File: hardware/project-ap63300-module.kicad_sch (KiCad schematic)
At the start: 12 parts, among them U2 AP63300WU-7

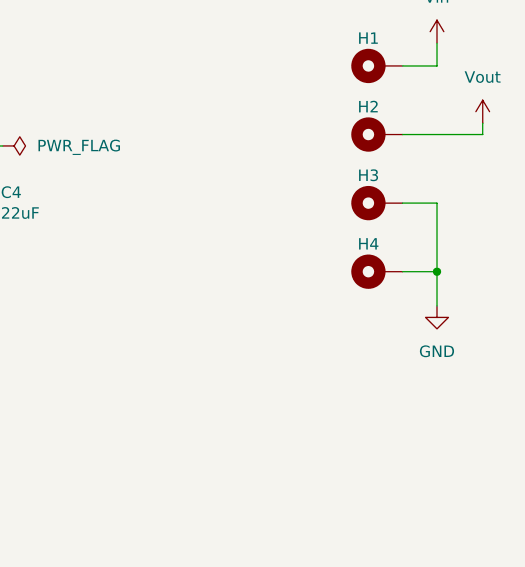
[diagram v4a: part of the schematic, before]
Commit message: Add labels
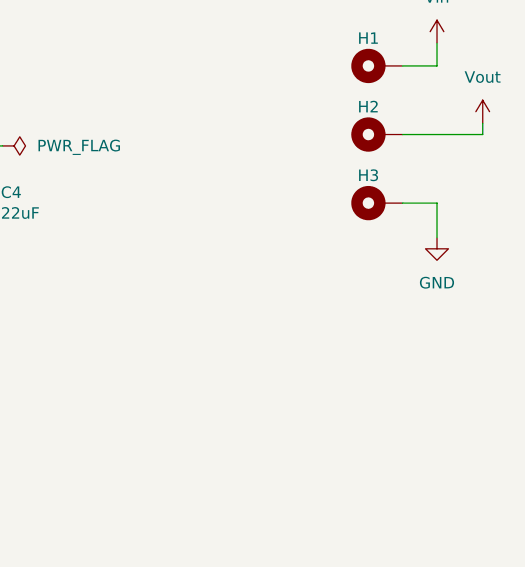
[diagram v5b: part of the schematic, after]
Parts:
- removed H4: MountingHole_Pad, MountingHole:MountingHole_2.2mm_M2_ISO14580_Pad, symbol Mechanical:MountingHole_Pad
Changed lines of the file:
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@@
-	)
-	(junction
-		(at 162.56 52.07)
-		(diameter 0)
-		(color 0 0 0 0)
 	)
 	(junction
@@
 	(wire
 		(pts
-			(xy 162.56 44.45) (xy 162.56 52.07)
-		)
-		(stroke
-			(width 0)
-			(type default)
-		)
-	)
-	(wire
-		(pts
 			(xy 67.31 43.18) (xy 69.85 43.18)
 		)
@@
 	(wire
 		(pts
-			(xy 162.56 52.07) (xy 162.56 55.88)
+			(xy 162.56 44.45) (xy 162.56 48.26)
 		)
 		(stroke
@@
 		(pts
 			(xy 68.58 33.02) (xy 67.31 33.02)
-		)
-		(stroke
-			(width 0)
-			(type default)
-		)
-	)
-	(wire
-		(pts
-			(xy 158.75 52.07) (xy 162.56 52.07)
 		)
 		(stroke
@@
 	)
 	(symbol
-		(lib_id "Mechanical:MountingHole_Pad")
-		(at 156.21 52.07 90)
-		(unit 1)
-		(exclude_from_sim yes)
-		(in_bom no)
-		(on_board yes)
-		(dnp no)
-		(property "Reference" "H4"
-			(at 154.94 49.022 90)
-			(effects
-				(font
-					(size 1.27 1.27)
-				)
-			)
-		)
-		(property "Value" "MountingHole_Pad"
-			(at 154.94 48.26 90)
-			(effects
-				(font
-					(size 1.27 1.27)
-				)
-				(hide yes)
-			)
-		)
-		(property "Footprint" "MountingHole:MountingHole_2.2mm_M2_ISO14580_Pad"
-			(at 156.21 52.07 0)
-			(effects
-				(font
-					(size 1.27 1.27)
-				)
-				(hide yes)
-			)
-		)
-		(property "Datasheet" "~"
-			(at 156.21 52.07 0)
-			(effects
-				(font
-					(size 1.27 1.27)
-				)
-				(hide yes)
-			)
-		)
-		(property "Description" "Mounting Hole with connection"
-			(at 156.21 52.07 0)
-			(effects
-				(font
-					(size 1.27 1.27)
-				)
-				(hide yes)
-			)
-		)
-		(pin "1"
-		)
-		(instances
-			(project ""
-				(path "/4d25b0a3-aea0-4711-9e74-24157a752b25"
-					(reference "H4")
-					(unit 1)
-				)
-			)
-		)
-	)
-	(symbol
 		(lib_id "power:GND")
-		(at 162.56 55.88 0)
+		(at 162.56 48.26 0)
 		(unit 1)
 		(exclude_from_sim no)
@@
 		(fields_autoplaced yes)
 		(property "Reference" "#PWR03"
-			(at 162.56 62.23 0)
+			(at 162.56 54.61 0)
 			(effects
 				(font
@@
 		)
 		(property "Value" "GND"
-			(at 162.56 60.96 0)
+			(at 162.56 53.34 0)
 			(effects
 				(font
@@
 		)
 		(property "Footprint" ""
-			(at 162.56 55.88 0)
+			(at 162.56 48.26 0)
 			(effects
 				(font
@@
 		)
 		(property "Datasheet" ""
-			(at 162.56 55.88 0)
+			(at 162.56 48.26 0)
 			(effects
 				(font
@@
 		)
 		(property "Description" "Power symbol creates a global label with name \"GND\" , ground"
-			(at 162.56 55.88 0)
-			(effects
-				(font
+			(at 162.56 48.26 0)
+			(effects
+				(font
